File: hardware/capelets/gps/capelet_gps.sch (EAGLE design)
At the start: 8 parts, among them IC1 SAM-M8Q, P1 SHPRD_CPLT_G, T1 SI2374DSSOT23-VSHAY

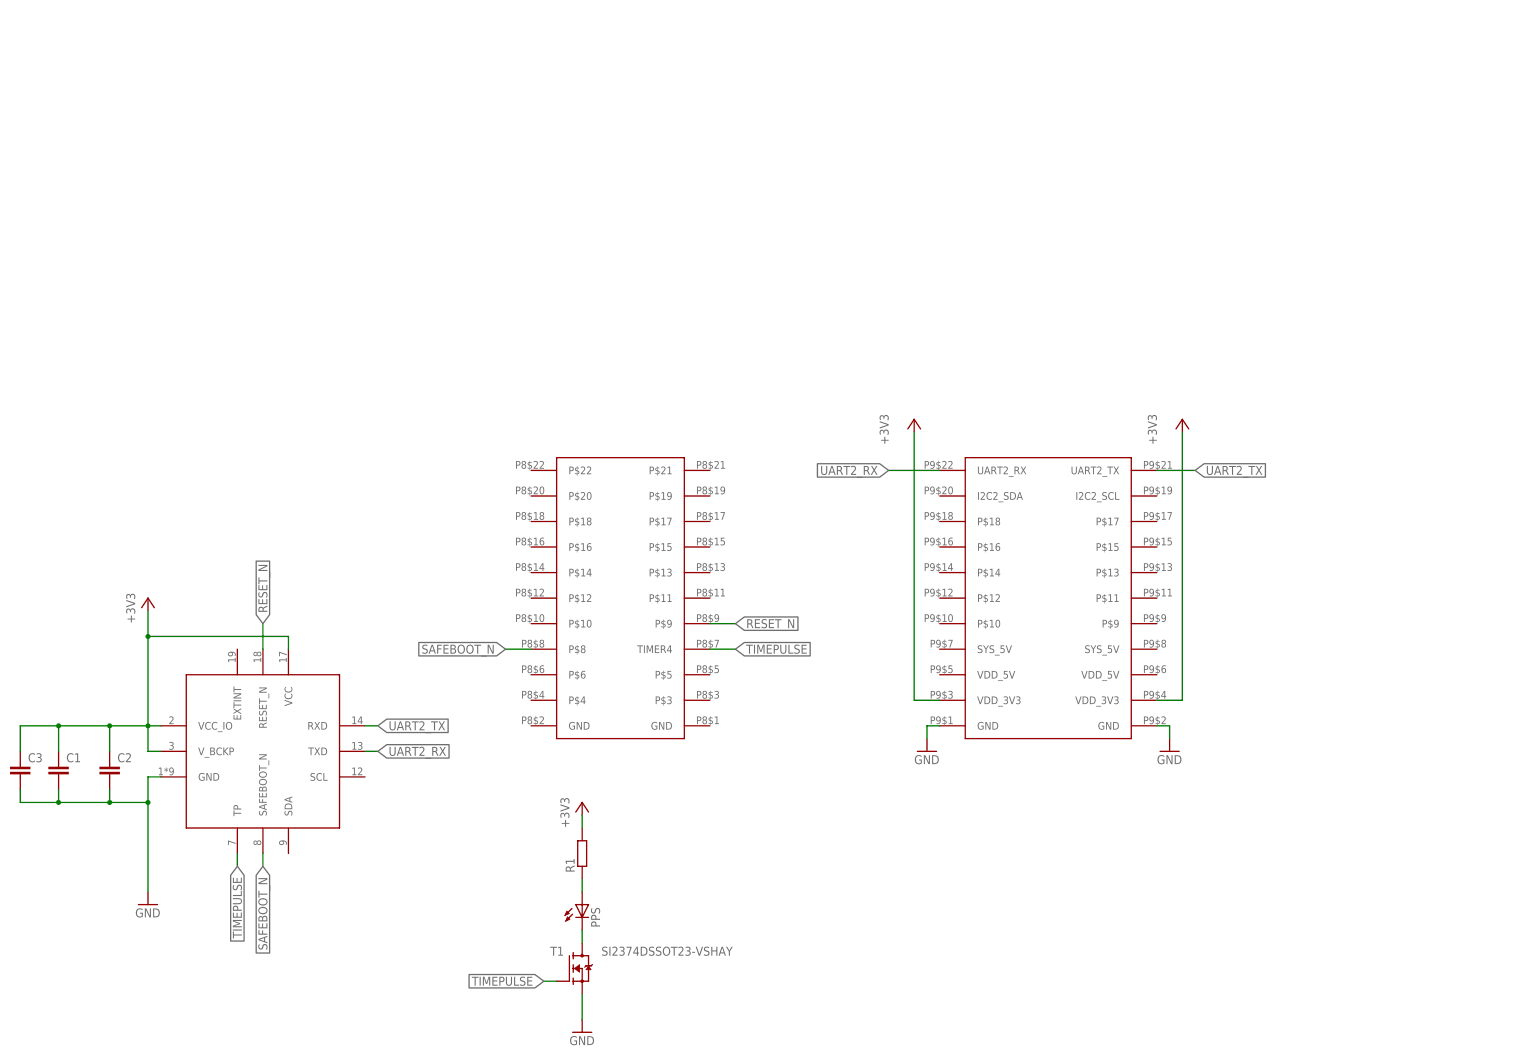
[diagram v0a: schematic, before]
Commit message: hardware: gps capelet: added component values and BOM
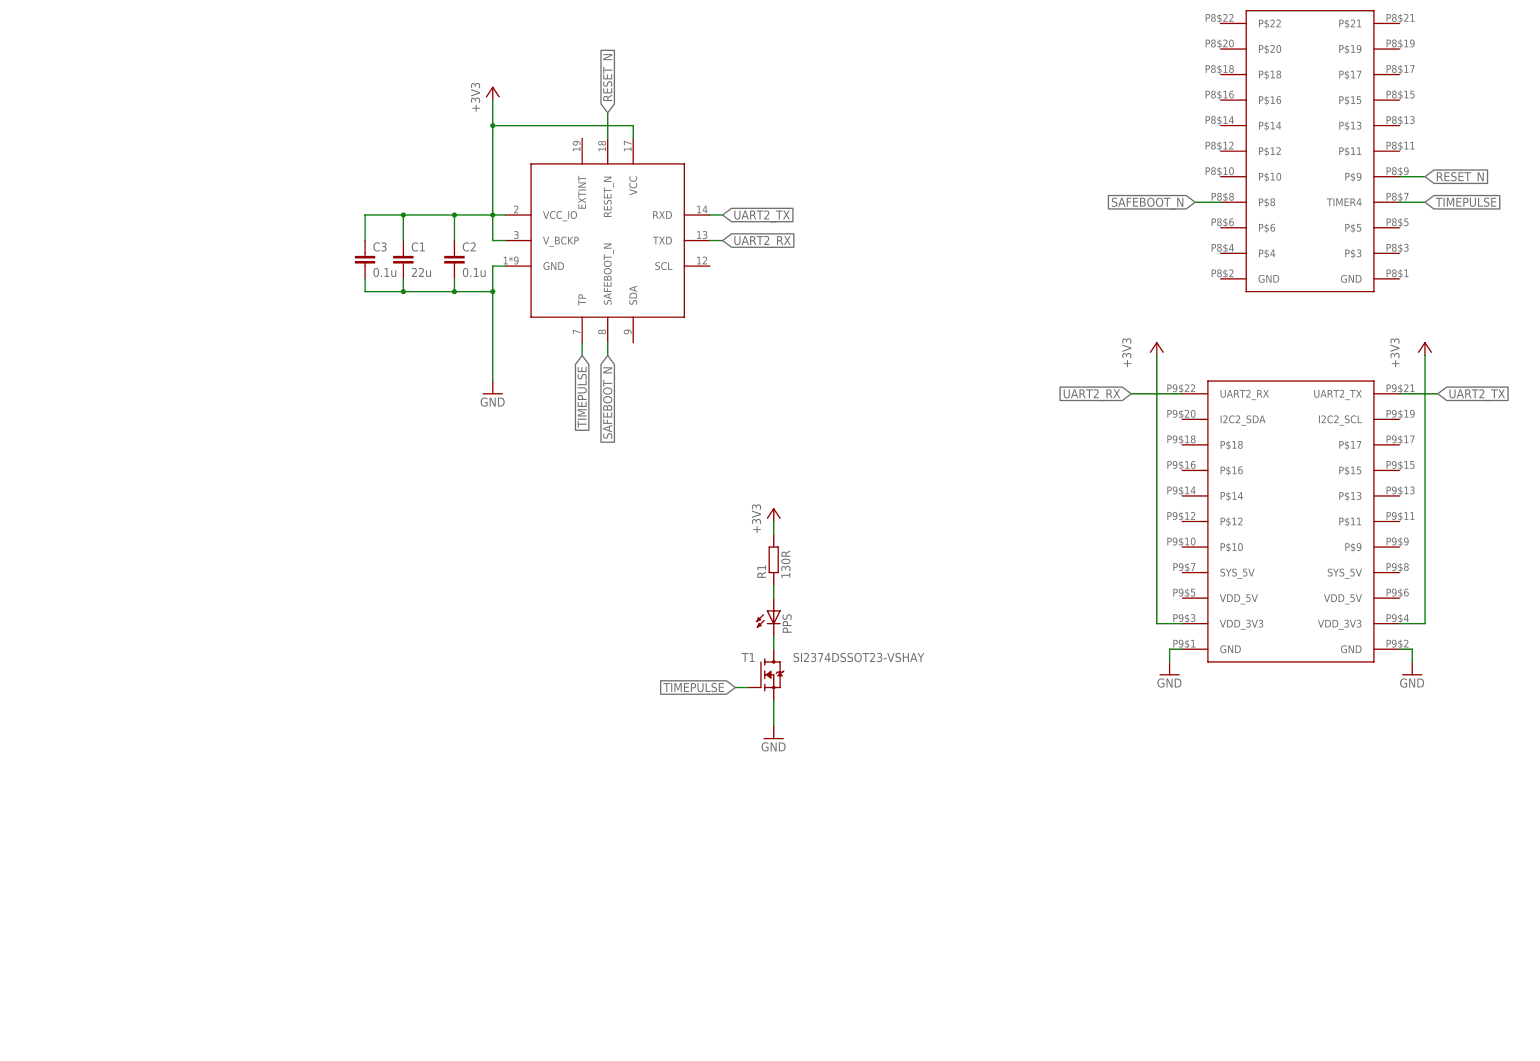
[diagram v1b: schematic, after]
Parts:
- C1: value (none) -> 22u
- C2, C3: value (none) -> 0.1u
- R1: value (none) -> 130R
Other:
- moved on the sheet: C1, C2, C3, PPS, R1, T1

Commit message: hardware: revised GPS capelet
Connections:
- net RESET_N: now also P1G$2.P$8; no longer P1G$2.P$9
- net SAFEBOOT_N: now also P1G$2.P$9; no longer P1G$2.P$8
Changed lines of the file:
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@@
 </segment>
 <segment>
-<pinref part="P1" gate="G$2" pin="P$9"/>
-<wire x1="231.14" y1="134.62" x2="236.22" y2="134.62" width="0.1524" layer="91"/>
-<label x="236.22" y="134.62" size="1.778" layer="95" xref="yes"/>
+<pinref part="P1" gate="G$2" pin="P$8"/>
+<wire x1="195.58" y1="129.54" x2="190.5" y2="129.54" width="0.1524" layer="91"/>
+<label x="190.5" y="129.54" size="1.778" layer="95" rot="R180" xref="yes"/>
 </segment>
 </net>
@@
 </segment>
 <segment>
-<pinref part="P1" gate="G$2" pin="P$8"/>
-<wire x1="195.58" y1="129.54" x2="190.5" y2="129.54" width="0.1524" layer="91"/>
-<label x="190.5" y="129.54" size="1.778" layer="95" rot="R180" xref="yes"/>
+<pinref part="P1" gate="G$2" pin="P$9"/>
+<wire x1="231.14" y1="134.62" x2="236.22" y2="134.62" width="0.1524" layer="91"/>
+<label x="236.22" y="134.62" size="1.778" layer="95" xref="yes"/>
 </segment>
 </net>
